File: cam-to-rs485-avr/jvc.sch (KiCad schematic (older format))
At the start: 29 parts

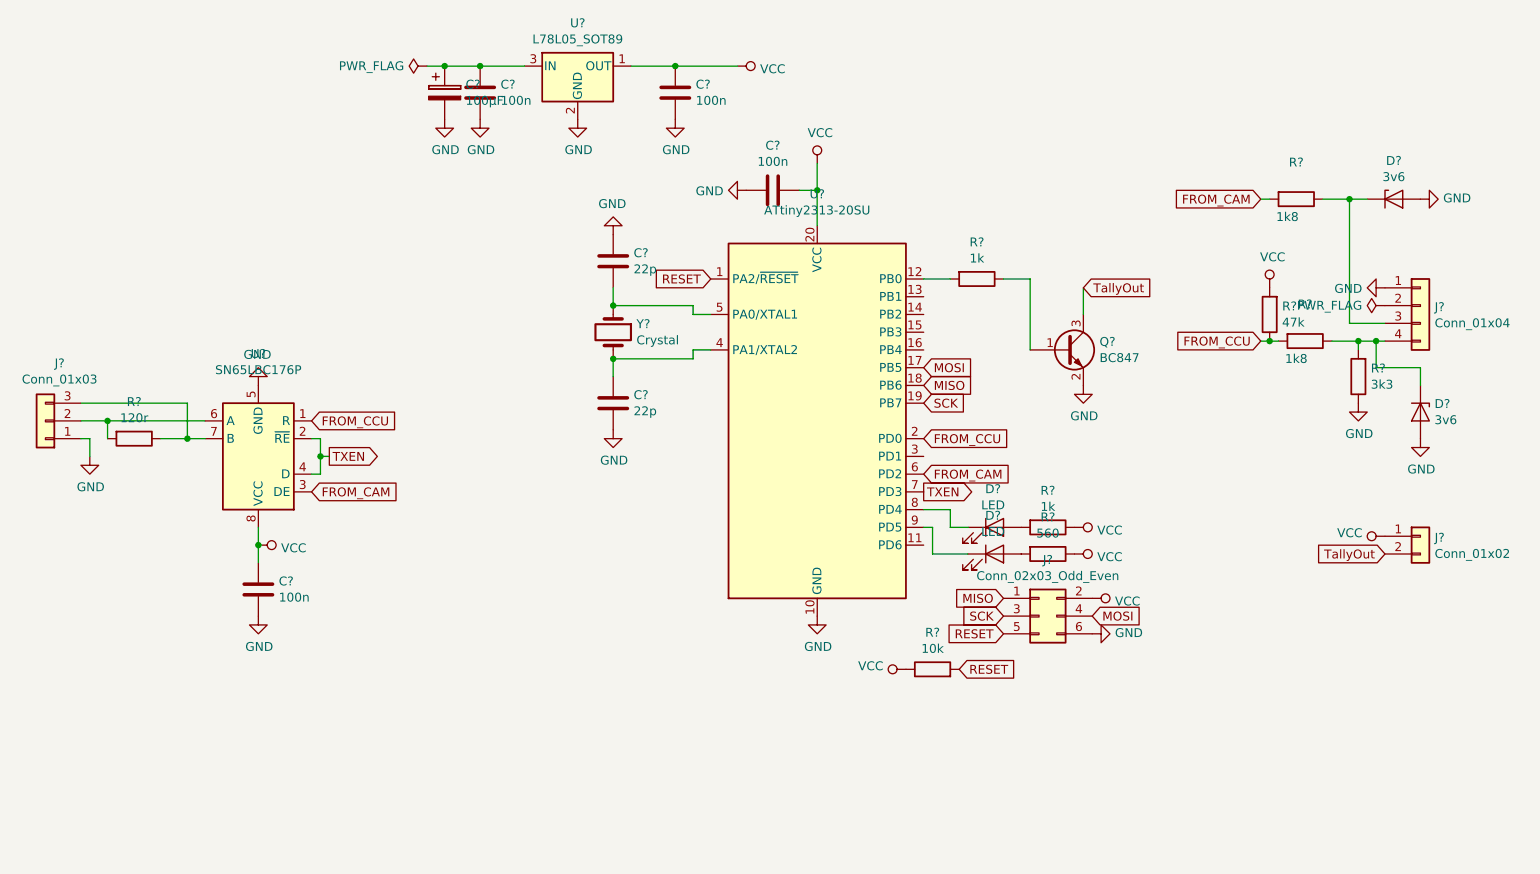
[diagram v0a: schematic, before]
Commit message: Assign footprints
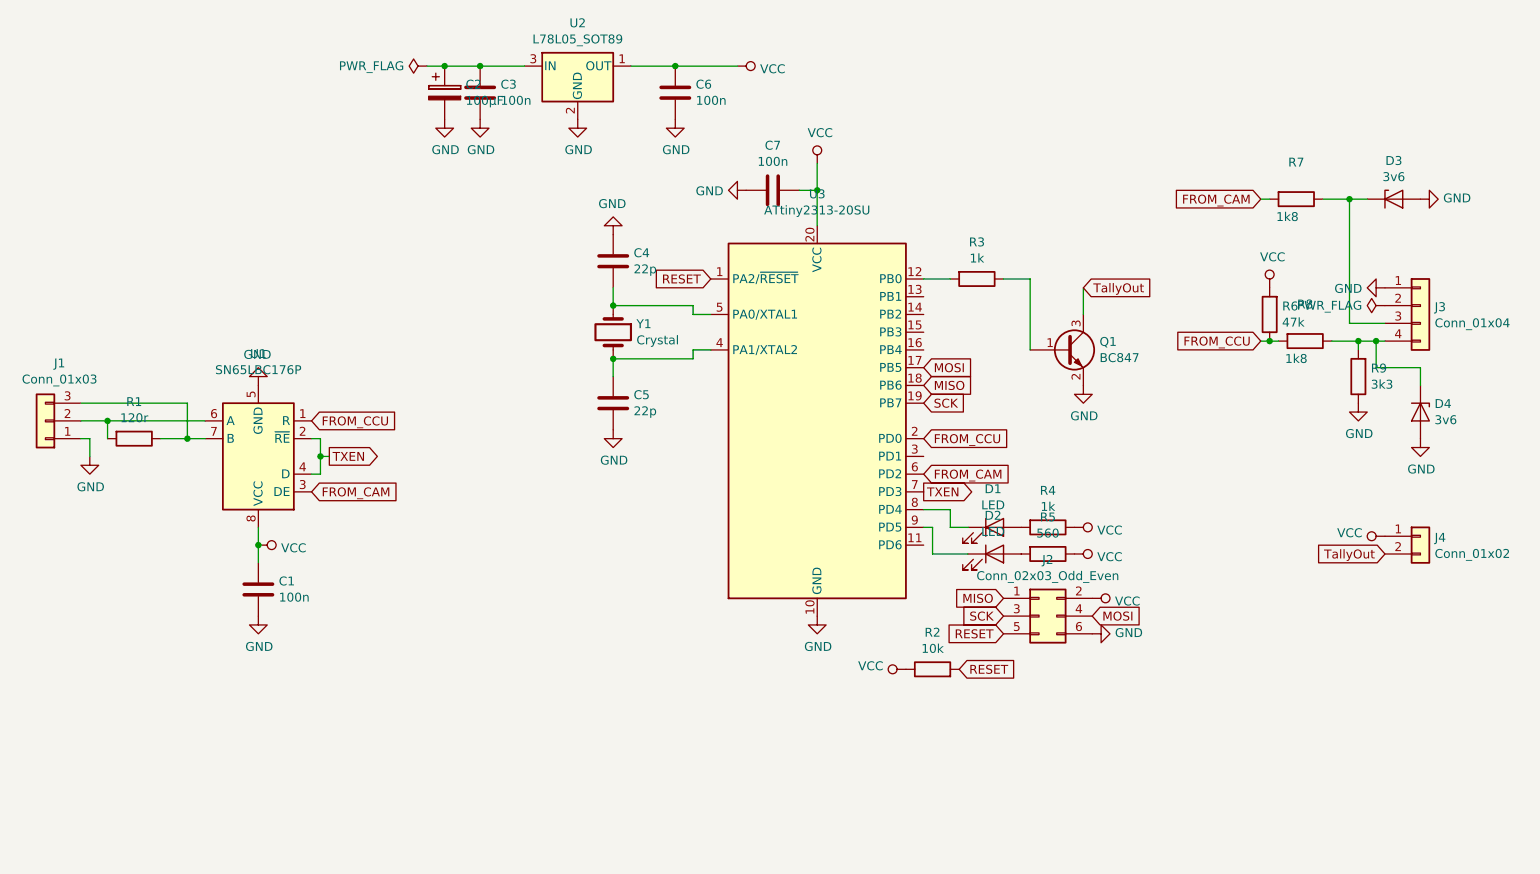
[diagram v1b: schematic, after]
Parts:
- C1, C3, C4, C5, C6, C7: renamed from C?; footprint (none) -> Capacitor_SMD:C_0805_2012Metric
- C2: renamed from C?; footprint (none) -> Capacitor_SMD:CP_Elec_10x10.5
- D1, D2: renamed from D?; footprint (none) -> LED_SMD:LED_0805_2012Metric
- D3, D4: renamed from D?; footprint (none) -> Diode_SMD:D_MELF-RM10_Universal_Handsoldering
- J1: renamed from J?; footprint (none) -> Connector_PinHeader_2.54mm:PinHeader_1x03_P2.54mm_Vertical
- J2: renamed from J?; footprint (none) -> Connector_PinHeader_2.54mm:PinHeader_2x03_P2.54mm_Vertical
- J3: renamed from J?; footprint (none) -> Connector_PinHeader_2.54mm:PinHeader_1x04_P2.54mm_Vertical
- J4: renamed from J?; footprint (none) -> Connector_PinHeader_2.54mm:PinHeader_1x02_P2.54mm_Vertical
- R1, R2, R3, R4, R5, R6, R7, R8, R9: renamed from R?; footprint (none) -> Resistor_SMD:R_0805_2012Metric
- Y1: renamed from Y?; footprint (none) -> Crystal:Crystal_SMD_HC49-SD
- gave numbers to parts that had none: 4

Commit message: pcb
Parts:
- removed U1: SN65LBC176P, Package_DIP:DIP-8_W7.62mm, symbol Interface_UART:SN65LBC176P
- added R10, R11: 0R, Resistor_SMD:R_1206_3216Metric, symbol Device:R
- added U1: MAX485E, Package_DIP:DIP-8_W7.62mm_Socket, symbol Interface_UART:MAX485E
- J2: footprint Connector_PinHeader_2.54mm:PinHeader_2x03_P2.54mm_Vertical -> Connector_PinHeader_2.54mm:PinHeader_2x03_P2.54mm_Vertical_SMD
- U3: symbol MCU_Microchip_ATtiny:ATtiny2313-20SU -> jvc-rescue:ATtiny2313-20SU-MCU_Microchip_ATtiny
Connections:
- net FROM_CAM: now also U1.4 (DI)
- net FROM_CCU: now also U1.1 (RO)
- net GND: now also R10.1, R10.2, R11.1, R11.2, U1.5 (GND)
- net TXEN: now also U1.2 (~RE), U1.3 (DE)
- net VCC: now also U1.8 (VCC)
- net at J1.2 (Pin_2): now also R1.1, U1.6 (A); no longer R1.2
- net at J1.3 (Pin_3): now also R1.2, U1.7 (B); no longer R1.1
- net +9V: now reaches C2.1, C3.1, U2.3 (IN)
- net +9V: now also J3.2 (Pin_2)
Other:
- moved on the sheet: C1, J1, R1
